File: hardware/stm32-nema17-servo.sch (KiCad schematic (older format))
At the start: 96 parts, among them J1 Conn_01x05, J2 C31-S-RA-CS1A-BK-SS, J3 TC-2050, J4 Screw_Terminal_01x02, J5 Screw_Terminal_01x02, J7 Conn_01x03, J8 Conn_01x03, J9 Conn_01x02, M1 Stepper_Motor_bipolar, Q1 NVTFS5C658NL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

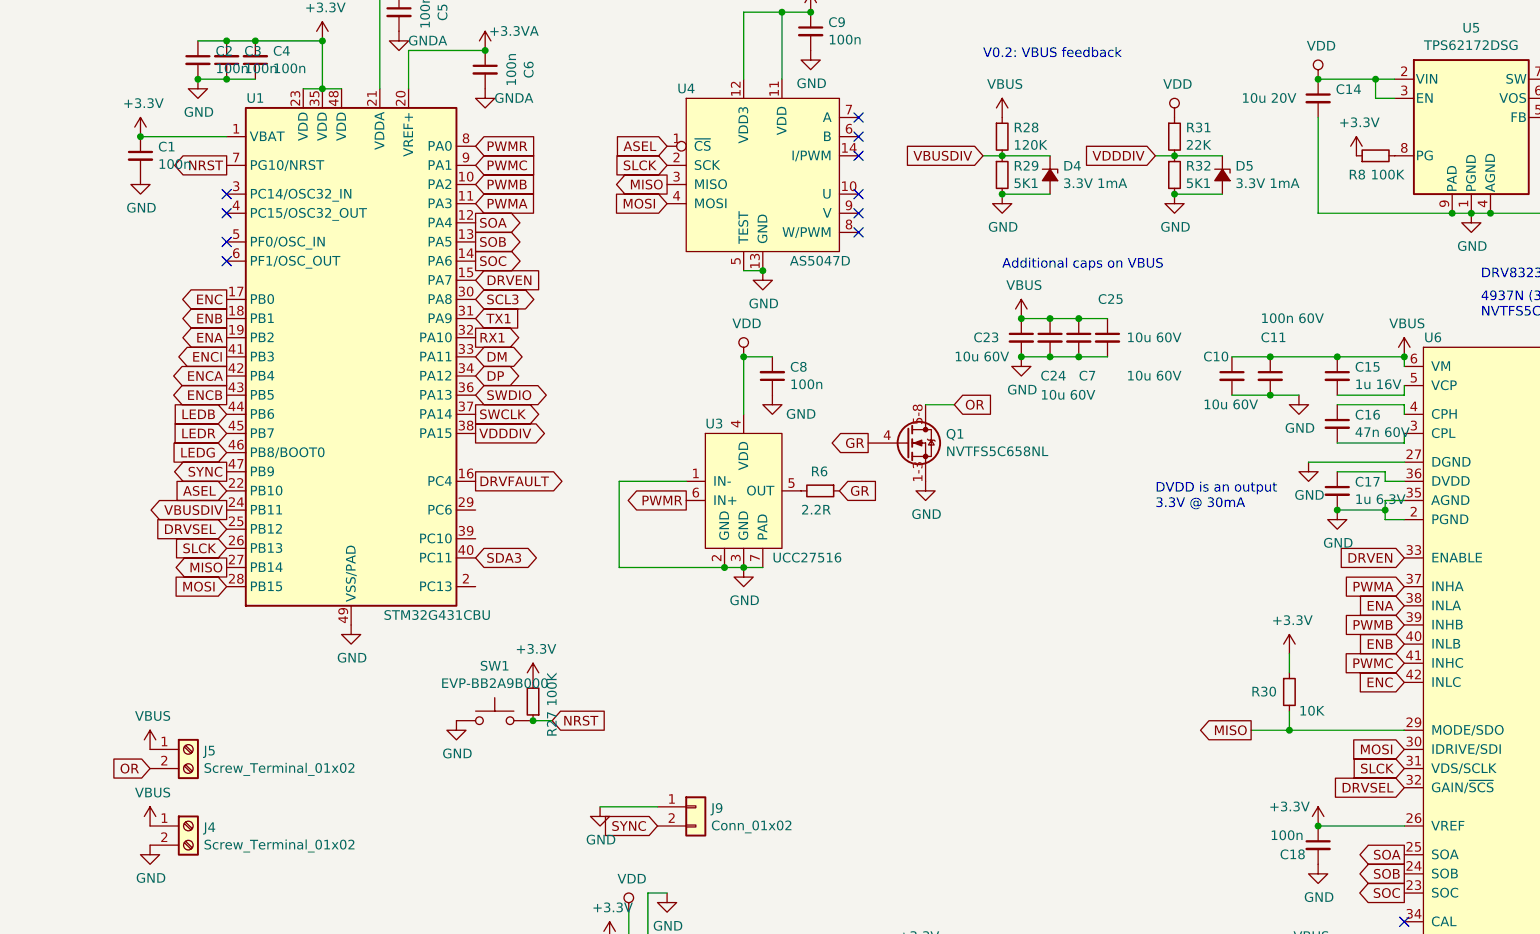
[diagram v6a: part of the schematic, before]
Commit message: more enhancements for v0.3, discovered that hardware NSS should be usable, after all
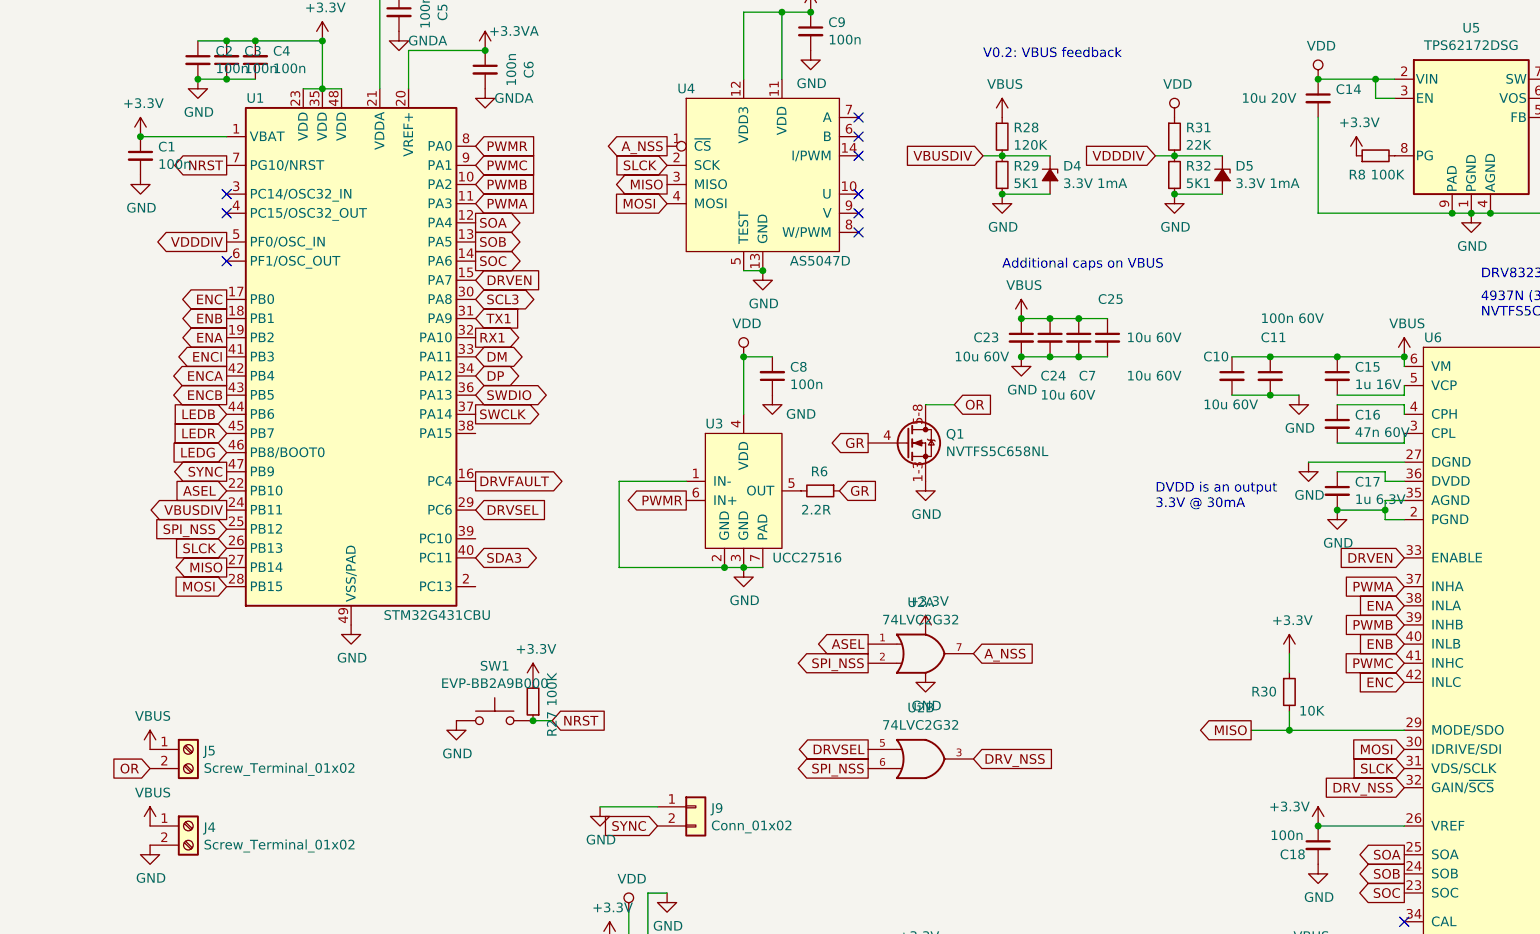
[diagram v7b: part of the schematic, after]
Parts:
- added U2: 74LVC2G32, Package_SON:X2SON-8_1.4x1mm_P0.35mm, symbol 74xGxx:74LVC2G32
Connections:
- net +3V3: now also U2.8 (VCC), U2.8 (VCC)
- net ASEL: now also U2.1; no longer U4.1 (~CS)
- net DRVSEL: now also U1.29 (PC6), U2.5; no longer U1.25 (PB12), U6.32 (GAIN/~SCS)
- net GND: now also U2.4 (GND), U2.4 (GND)
- net VDDDIV: now also U1.5 (PF0/OSC_IN); no longer U1.38 (PA15)
- new net A_NSS: U2.7, U4.1 (~CS)
- new net DRV_NSS: U2.3, U6.32 (GAIN/~SCS)
- new net SPI_NSS: U1.25 (PB12), U2.2, U2.6
- no-connect marks 13 -> 12
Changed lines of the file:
@@
 SLCK
 Text GLabel 7450 4950 0    50   Input ~ 0
-DRVSEL
-Text GLabel 3600 1600 0    50   Input ~ 0
-ASEL
+DRV_NSS
+Text GLabel 3600 1600 0    50   Output ~ 0
+A_NSS
 Text GLabel 2600 1900 2    50   Input ~ 0
 PWMA
@@
 	3150 6300 3550 6300
 Connection ~ 3150 6300
-Text GLabel 1300 3600 0    50   Input ~ 0
+Text GLabel 2600 3500 2    50   Input ~ 0
 DRVSEL
 Text GLabel 1300 3400 0    50   Input ~ 0
@@
 RX1
 NoConn ~ 1300 2200
-NoConn ~ 1300 2100
 NoConn ~ 1300 1950
 NoConn ~ 1300 1850
@@
 	5600 2700 5750 2700
 Connection ~ 5600 2700
-Text GLabel 2600 3100 2    50   Output ~ 0
+Text GLabel 1300 2100 0    50   Output ~ 0
 VDDDIV
 $Comp
@@
 	1    0    0    -1
 $EndComp
+Text GLabel 1300 3600 0    50   Input ~ 0
+SPI_NSS
+$Comp
+L 74xGxx:74LVC2G32 U2
+U 1 1 5E9B48D8
+P 4950 4250
+F 0 "U2" H 4925 4517 50  0000 C CNN
+F 1 "74LVC2G32" H 4925 4426 50  0000 C CNN
+F 2 "Package_SON:X2SON-8_1.4x1mm_P0.35mm" H 4950 4250 50  0001 C CNN
+F 3 "http://www.ti.com/lit/sg/scyt129e/scyt129e.pdf" H 4950 4250 50  0001 C CNN
+	1    4950 4250
+	1    0    0    -1
+$EndComp
+$Comp
+L 74xGxx:74LVC2G32 U2
+U 2 1 5E9B5DA5
+P 4950 4800
+F 0 "U2" H 4925 5067 50  0000 C CNN
+F 1 "74LVC2G32" H 4925 4976 50  0000 C CNN
+F 2 "Package_SON:X2SON-8_1.4x1mm_P0.35mm" H 4950 4800 50  0001 C CNN
+F 3 "http://www.ti.com/lit/sg/scyt129e/scyt129e.pdf" H 4950 4800 50  0001 C CNN
+	2    4950 4800
+	1    0    0    -1
+$EndComp
+Text GLabel 4650 4200 0    50   Output ~ 0
+ASEL
+Text GLabel 4650 4300 0    50   Output ~ 0
+SPI_NSS
+Text GLabel 4650 4750 0    50   Output ~ 0
+DRVSEL
+Text GLabel 4650 4850 0    50   Output ~ 0
+SPI_NSS
+Text GLabel 5200 4250 2    50   Input ~ 0
+A_NSS
+Text GLabel 5200 4800 2    50   Input ~ 0
+DRV_NSS
+$Comp
+L power:+3.3V #PWR0112
+U 1 1 5EA38885
+P 4950 4150
+F 0 "#PWR0112" H 4950 4000 50  0001 C CNN
+F 1 "+3.3V" H 4965 4323 50  0000 C CNN
+F 2 "" H 4950 4150 50  0001 C CNN
+F 3 "" H 4950 4150 50  0001 C CNN
+	1    4950 4150
+	1    0    0    -1
+$EndComp
+$Comp
+L power:GND #PWR0113
+U 1 1 5EA4680D
+P 4950 4350
+F 0 "#PWR0113" H 4950 4100 50  0001 C CNN
+F 1 "GND" H 4955 4177 50  0000 C CNN
+F 2 "" H 4950 4350 50  0001 C CNN
+F 3 "" H 4950 4350 50  0001 C CNN
+	1    4950 4350
+	1    0    0    -1
+$EndComp

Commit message: hardware v0.3 as ordered
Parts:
- removed U2: 74LVC2G32, Package_SON:X2SON-8_1.4x1mm_P0.35mm, symbol 74xGxx:74LVC2G32
- added R33, R34: 1K, Resistor_SMD:R_0402_1005Metric, symbol Device:R_Small
- U5: symbol Regulator_Switching:TPS62172DSG -> stm32-nema17:TPS62172DSG
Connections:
- net A_NSS is gone; now on net ASEL: U4.1 (~CS)
- net DRV_NSS is gone; now on net DRVSEL: U6.32 (GAIN/~SCS)
- net ASEL: now also R33.2
- net DRVSEL: now also R34.2
- net SPI_NSS: now also R33.1, R34.1
- no-connect marks 12 -> 17
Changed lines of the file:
@@
 L power:+3.3V #PWR045
 U 1 1 5D583C48
-P 8900 1250
-F 0 "#PWR045" H 8900 1100 50  0001 C CNN
-F 1 "+3.3V" H 8915 1423 50  0000 C CNN
-F 2 "" H 8900 1250 50  0001 C CNN
-F 3 "" H 8900 1250 50  0001 C CNN
-	1    8900 1250
+P 8900 1000
+F 0 "#PWR045" H 8900 850 50  0001 C CNN
+F 1 "+3.3V" H 8950 1150 50  0000 C CNN
+F 2 "" H 8900 1000 50  0001 C CNN
+F 3 "" H 8900 1000 50  0001 C CNN
+	1    8900 1000
 	1    0    0    -1
 $EndComp
@@
 $EndComp
 $Comp
-L Regulator_Switching:TPS62172DSG U5
+L stm32-nema17:TPS62172DSG U5
 U 1 1 5D684E5E
 P 7800 1550
@@
 L power:VDD #PWR057
 U 1 1 5D6A08F4
-P 10550 6050
-F 0 "#PWR057" H 10550 5900 50  0001 C CNN
-F 1 "VDD" H 10567 6223 50  0000 C CNN
-F 2 "" H 10550 6050 50  0001 C CNN
-F 3 "" H 10550 6050 50  0001 C CNN
-	1    10550 6050
+P 10550 5950
+F 0 "#PWR057" H 10550 5800 50  0001 C CNN
+F 1 "VDD" H 10550 6100 50  0000 C CNN
+F 2 "" H 10550 5950 50  0001 C CNN
+F 3 "" H 10550 5950 50  0001 C CNN
+	1    10550 5950
 	1    0    0    -1
 $EndComp
@@
 	8550 1250 8500 1250
 Wire Wire Line
-	8550 1250 8900 1250
+	8550 1250 8700 1250
 Connection ~ 8550 1250
 Wire Wire Line
@@
 SPI_NSS
 $Comp
-L 74xGxx:74LVC2G32 U2
+L 74xGxx:74LVC2G32 #U2
 U 1 1 5E9B48D8
 P 4950 4250
-F 0 "U2" H 4925 4517 50  0000 C CNN
-F 1 "74LVC2G32" H 4925 4426 50  0000 C CNN
+F 0 "#U2" H 5100 4350 50  0000 C CNN
+F 1 "74LVC2G32" H 5250 4150 50  0000 C CNN
 F 2 "Package_SON:X2SON-8_1.4x1mm_P0.35mm" H 4950 4250 50  0001 C CNN
 F 3 "http://www.ti.com/lit/sg/scyt129e/scyt129e.pdf" H 4950 4250 50  0001 C CNN
@@
 $EndComp
 $Comp
-L 74xGxx:74LVC2G32 U2
+L 74xGxx:74LVC2G32 #U2
 U 2 1 5E9B5DA5
 P 4950 4800
-F 0 "U2" H 4925 5067 50  0000 C CNN
-F 1 "74LVC2G32" H 4925 4976 50  0000 C CNN
+F 0 "#U2" H 5100 4900 50  0000 C CNN
+F 1 "74LVC2G32" H 5250 4700 50  0000 C CNN
 F 2 "Package_SON:X2SON-8_1.4x1mm_P0.35mm" H 4950 4800 50  0001 C CNN
 F 3 "http://www.ti.com/lit/sg/scyt129e/scyt129e.pdf" H 4950 4800 50  0001 C CNN
@@
 P 4950 4150
 F 0 "#PWR0112" H 4950 4000 50  0001 C CNN
-F 1 "+3.3V" H 4965 4323 50  0000 C CNN
+F 1 "+3.3V" H 4950 4300 50  0000 C CNN
 F 2 "" H 4950 4150 50  0001 C CNN
 F 3 "" H 4950 4150 50  0001 C CNN
@@
 	1    0    0    -1
 $EndComp
+$Comp
+L Device:R_Small R34
+U 1 1 5EB5A348
+P 5800 5500
+F 0 "R34" H 5650 5600 50  0000 L CNN
+F 1 "1K" H 5650 5500 50  0000 L CNN
+F 2 "Resistor_SMD:R_0402_1005Metric" H 5800 5500 50  0001 C CNN
+F 3 "~" H 5800 5500 50  0001 C CNN
+F 4 "RC0402JR-07680RL" H 5800 5500 50  0001 C CNN "MPN"
+	1    5800 5500
+	-1   0    0    1
+$EndComp
+Text GLabel 5650 5600 0    50   Output ~ 0
+SPI_NSS
+Text GLabel 5650 5400 0    50   Output ~ 0
+DRVSEL
+Text GLabel 5950 5400 2    50   Input ~ 0
+DRV_NSS
+Wire Wire Line
+	5650 5400 5800 5400
+Wire Wire Line
+	5650 5600 5800 5600
+Wire Wire Line
+	5800 5400 5950 5400
+Connection ~ 5800 5400
+$Comp
+L Device:R_Small R33
+U 1 1 5EB9495A
+P 5800 5150
+F 0 "R33" H 5650 5250 50  0000 L CNN
+F 1 "1K" H 5650 5150 50  0000 L CNN
+F 2 "Resistor_SMD:R_0402_1005Metric" H 5800 5150 50  0001 C CNN
+F 3 "~" H 5800 5150 50  0001 C CNN
+F 4 "RC0402JR-07680RL" H 5800 5150 50  0001 C CNN "MPN"
+	1    5800 5150
+	-1   0    0    1
+$EndComp
+Text GLabel 5650 5250 0    50   Output ~ 0
+SPI_NSS
+Text GLabel 5950 5050 2    50   Input ~ 0
+A_NSS
+Text GLabel 5650 5050 0    50   Output ~ 0
+ASEL
+Wire Wire Line
+	5650 5050 5800 5050
+Wire Wire Line
+	5800 5050 5950 5050
+Connection ~ 5800 5050
+Wire Wire Line
+	5650 5250 5800 5250
+$Comp
+L power:PWR_FLAG #FLG0101
+U 1 1 5EC48EB2
+P 8700 1000
+F 0 "#FLG0101" H 8700 1075 50  0001 C CNN
+F 1 "PWR_FLAG" H 8600 1150 50  0000 C CNN
+F 2 "" H 8700 1000 50  0001 C CNN
+F 3 "~" H 8700 1000 50  0001 C CNN
+	1    8700 1000
+	1    0    0    -1
+$EndComp
+Wire Wire Line
+	8700 1000 8700 1250
+Connection ~ 8700 1250
+Wire Wire Line
+	8700 1250 8900 1250
+$Comp
+L power:PWR_FLAG #FLG0102
+U 1 1 5EC59C6A
+P 10800 5950
+F 0 "#FLG0102" H 10800 6025 50  0001 C CNN
+F 1 "PWR_FLAG" H 10950 6100 50  0000 C CNN
+F 2 "" H 10800 5950 50  0001 C CNN
+F 3 "~" H 10800 5950 50  0001 C CNN
+	1    10800 5950
+	1    0    0    -1
+$EndComp
+Wire Wire Line
+	10800 5950 10800 6050
+Wire Wire Line
+	10800 6050 10550 6050
+Wire Wire Line
+	10550 5950 10550 6050
+Wire Wire Line
+	8900 1000 8900 1250
+$Comp
+L power:GND #PWR0115
+U 1 1 5EC9B8D2
+P 9700 1400
+F 0 "#PWR0115" H 9700 1150 50  0001 C CNN
+F 1 "GND" H 9705 1227 50  0000 C CNN
+F 2 "" H 9700 1400 50  0001 C CNN
+F 3 "" H 9700 1400 50  0001 C CNN
+	1    9700 1400
+	1    0    0    -1
+$EndComp
+$Comp
+L power:PWR_FLAG #FLG0103
+U 1 1 5ECAD091
+P 9700 1400
+F 0 "#FLG0103" H 9700 1475 50  0001 C CNN
+F 1 "PWR_FLAG" H 9700 1550 50  0000 C CNN
+F 2 "" H 9700 1400 50  0001 C CNN
+F 3 "~" H 9700 1400 50  0001 C CNN
+	1    9700 1400
+	1    0    0    -1
+$EndComp
+$Comp
+L power:PWR_FLAG #FLG0104
+U 1 1 5ECBD395
+P 1550 5850
+F 0 "#FLG0104" H 1550 5925 50  0001 C CNN
+F 1 "PWR_FLAG" H 1550 6023 50  0000 C CNN
+F 2 "" H 1550 5850 50  0001 C CNN
+F 3 "~" H 1550 5850 50  0001 C CNN
+	1    1550 5850
+	1    0    0    -1
+$EndComp
+Wire Wire Line
+	1550 5850 1550 6050
+Connection ~ 1550 6050
+NoConn ~ 1550 7150
+NoConn ~ 1550 7250
+$Comp
+L power:PWR_FLAG #FLG0105
+U 1 1 5ED0A8D6
+P 9250 750
+F 0 "#FLG0105" H 9250 825 50  0001 C CNN
+F 1 "PWR_FLAG" H 9000 800 50  0000 C CNN
+F 2 "" H 9250 750 50  0001 C CNN
+F 3 "~" H 9250 750 50  0001 C CNN
+	1    9250 750
+	1    0    0    -1
+$EndComp
+Wire Wire Line
+	9250 750  9350 750
+Connection ~ 9350 750
+NoConn ~ 2600 3100
+NoConn ~ 2600 3650
+NoConn ~ 2600 3900
 $EndSCHEMATC
